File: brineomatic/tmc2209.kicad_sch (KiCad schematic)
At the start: 19 parts, among them J20 Conn_01x04, U9 TMC2209-LA

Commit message: updated jlc parts rotations and placement offsets
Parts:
- C39: LCSC C4967 -> C21122
- C42, J20: Rotation Offset (none) -> 180
- R53, U9: Rotation Offset (none) -> 270
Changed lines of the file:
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@@
+			)
+		)
+		(property "Rotation Offset" "180"
+			(at 152.4 57.15 0)
+			(effects
+				(font
+					(size 1.27 1.27)
+				)
+				(hide yes)
 			)
 		)
@@
 			)
 		)
+		(property "Rotation Offset" "270"
+			(at 81.28 105.41 0)
+			(effects
+				(font
+					(size 1.27 1.27)
+				)
+				(hide yes)
+			)
+		)
 		(pin "9"
 		)
@@
 		)
 		(property "LCSC" "C157926"
+			(at 109.22 110.49 0)
+			(effects
+				(font
+					(size 1.27 1.27)
+				)
+				(hide yes)
+			)
+		)
+		(property "Rotation Offset" "180"
 			(at 109.22 110.49 0)
 			(effects
@@
 			)
 		)
-		(property "LCSC" "C4967"
+		(property "LCSC" "C21122"
 			(at 104.14 95.25 90)
 			(effects
@@
 			(at 134.62 90.17 90)
 			(effects
+				(font
+					(size 1.27 1.27)
+				)
+				(hide yes)
+			)
+		)
+		(property "Rotation Offset" "270"
+			(at 134.62 90.17 90)
+			(effects

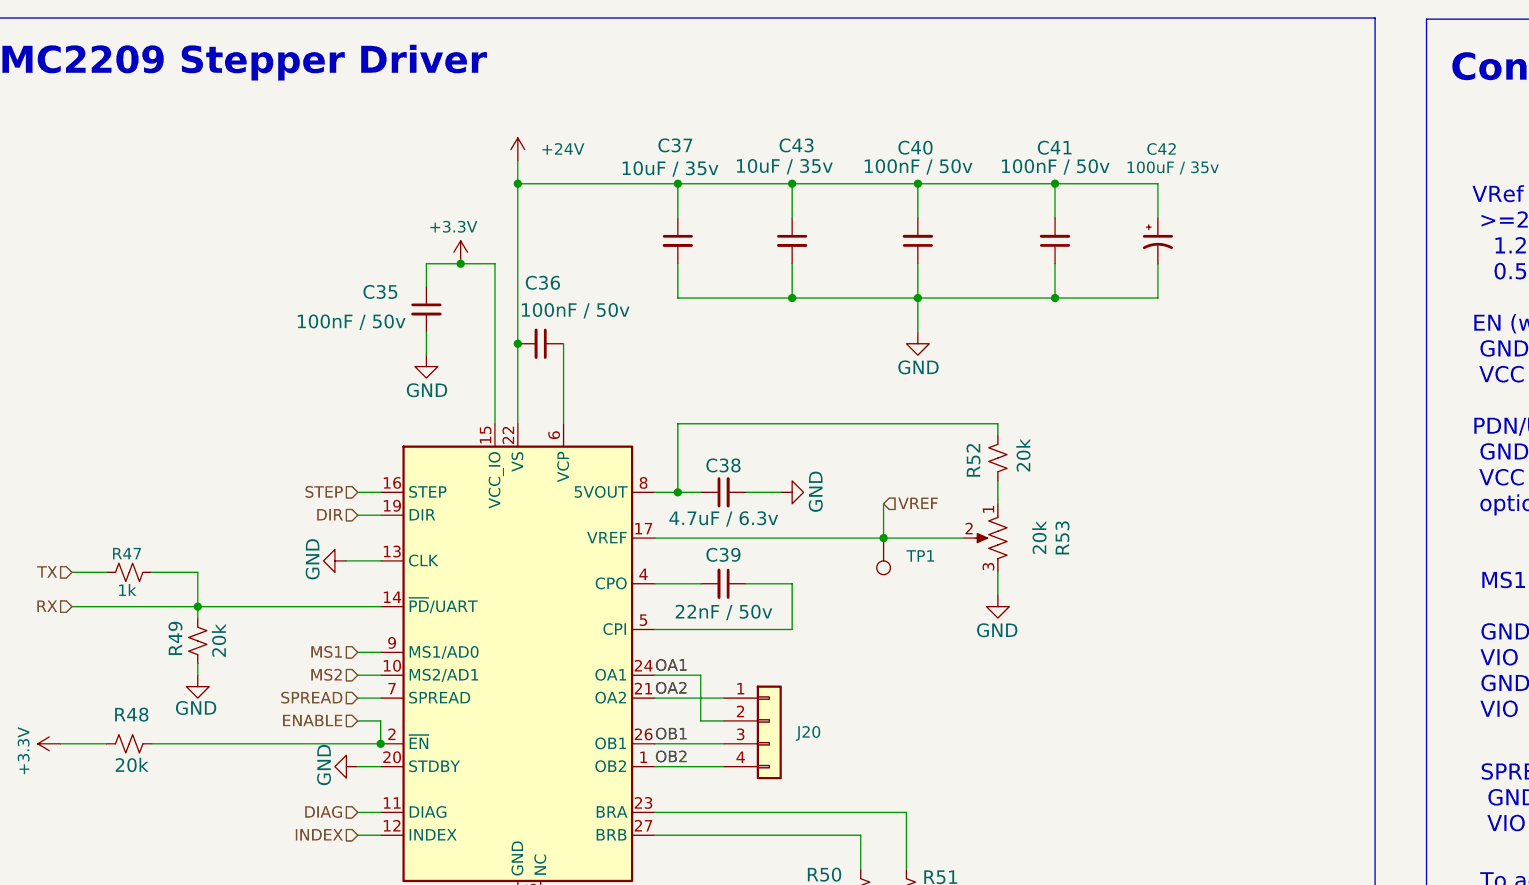
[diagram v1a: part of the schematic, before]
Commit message: via stitching, a couple minor changes, i think its ready for production
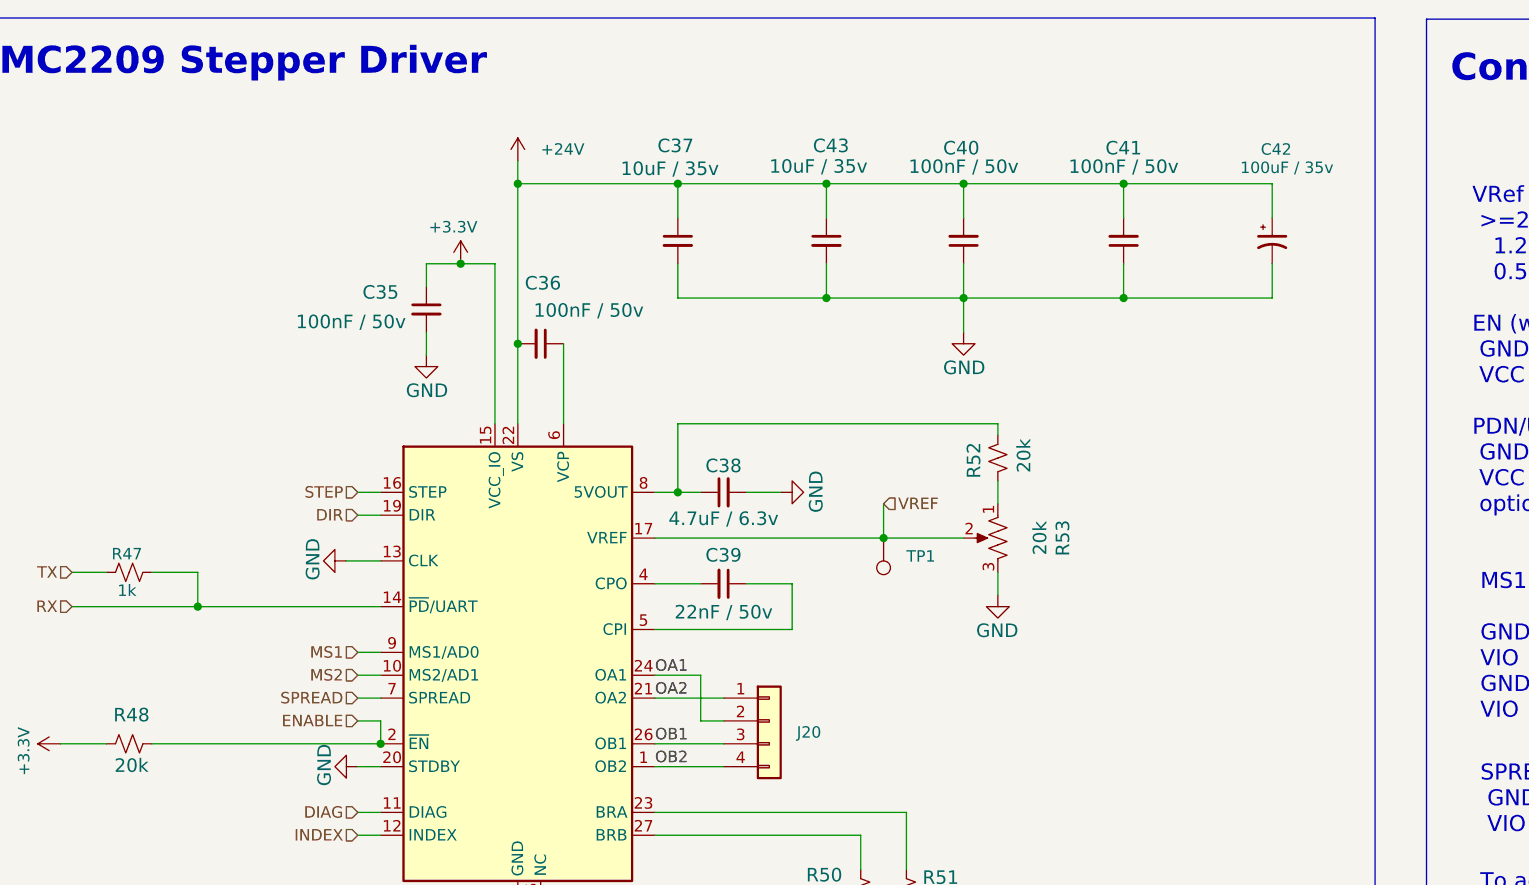
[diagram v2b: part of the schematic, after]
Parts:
- removed R49: 20k, Resistor_SMD:R_0603_1608Metric, symbol Device:R_Small_US
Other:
- moved on the sheet: C40, C41, C42, C43

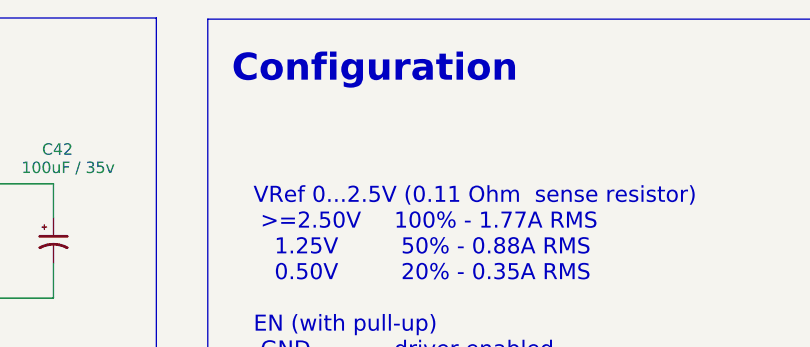
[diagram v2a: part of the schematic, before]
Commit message: added qwiic i2c connector
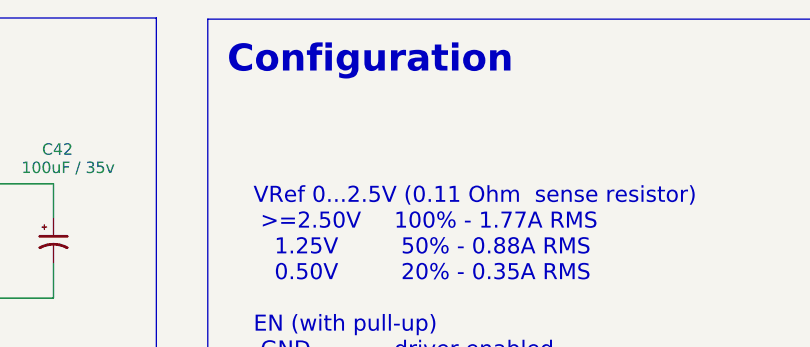
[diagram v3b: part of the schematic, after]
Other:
- title: (none) -> https://github.com/hoeken/brineomatic
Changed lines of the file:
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@@
 	(generator_version "9.0")
 	(paper "A4")
+	(title_block
+		(title "https://github.com/hoeken/brineomatic")
+		(date "2025-08-28")
+		(rev "B")
+	)
 	(rectangle
 		(start 18.415 32.385)
@@
 	(text "Configuration"
 		(exclude_from_sim no)
-		(at 184.912 38.1 0)
+		(at 184.404 37.084 0)
 		(effects
 			(font

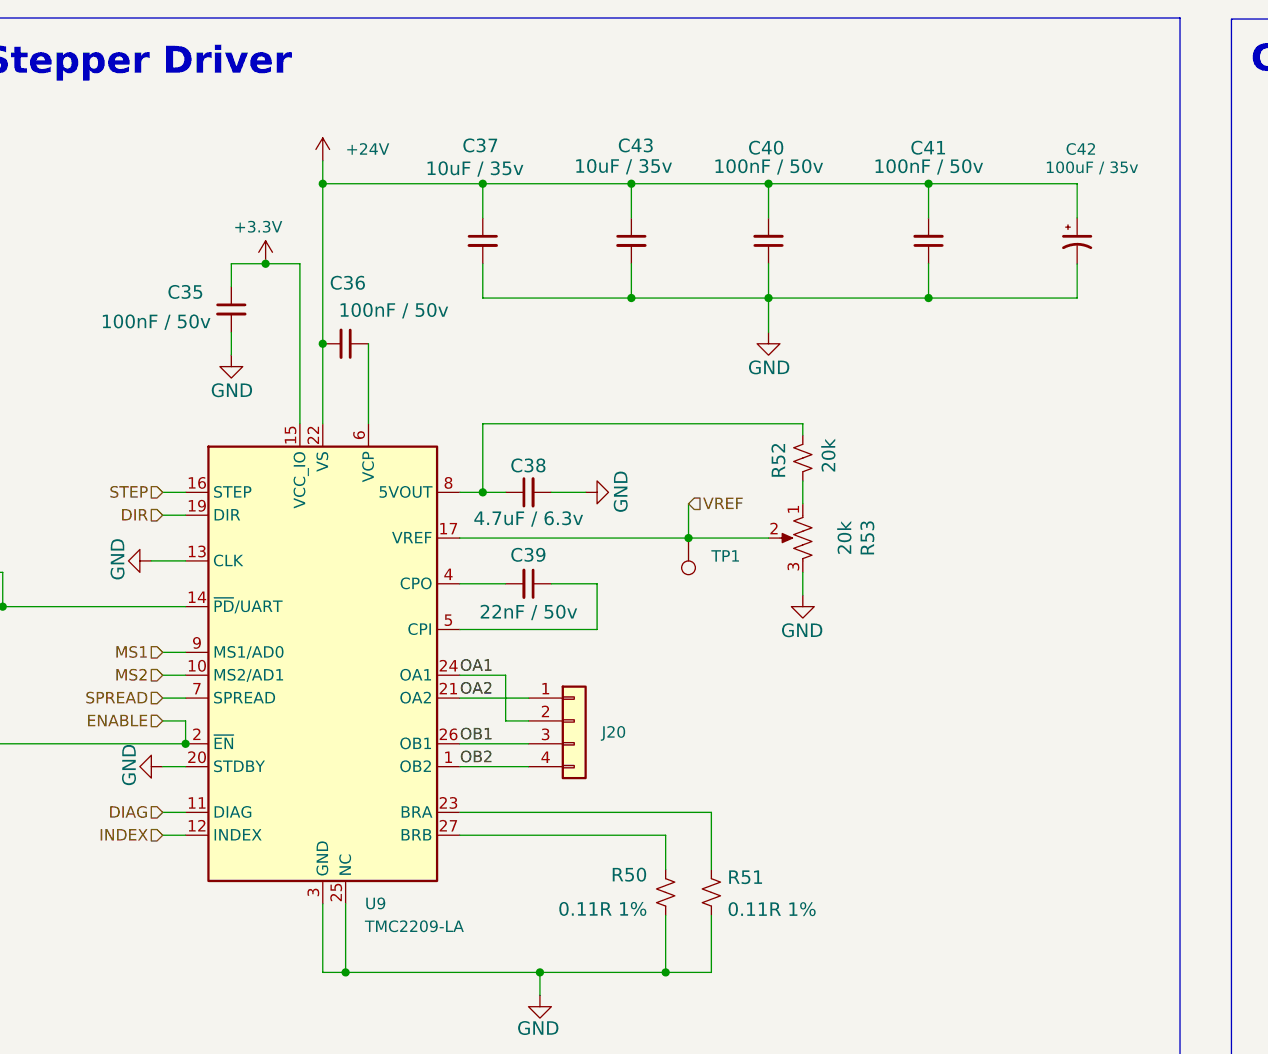
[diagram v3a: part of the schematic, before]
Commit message: added pullup resistor to adc alert
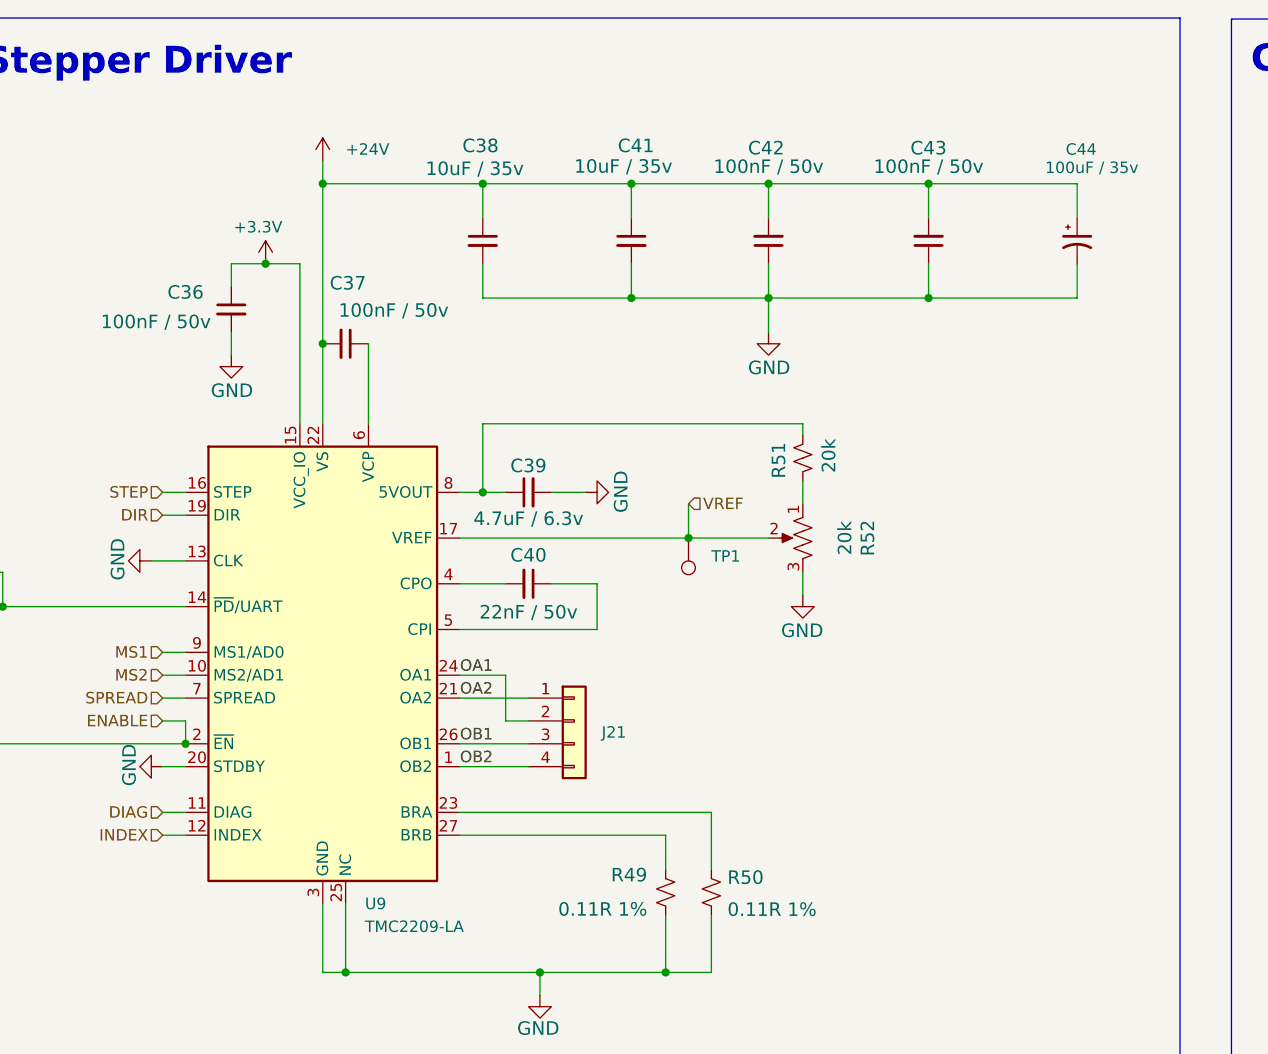
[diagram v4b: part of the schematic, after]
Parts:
- renumbered C35 to C36, C36 to C37, C37 to C38, C38 to C39, C39 to C40, C43 to C41, C40 to C42, C41 to C43, C42 to C44, J20 to J21, R50 to R49, R51 to R50, R52 to R51, R53 to R52
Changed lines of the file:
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@@
 		(on_board yes)
 		(dnp no)
-		(property "Reference" "#GND08"
+		(property "Reference" "#GND07"
 			(at 134.62 96.52 0)
 			(effects
@@
 			(project "brineomatic"
 				(path "/96477ae2-ef08-48f3-8dd4-fe4478541f68/0f01c39f-0c25-414e-9ed3-1ba09e2af0c5"
-					(reference "#GND08")
+					(reference "#GND07")
 					(unit 1)
 				)
@@
 		(on_board yes)
 		(dnp no)
-		(property "Reference" "#GND06"
+		(property "Reference" "#GND05"
 			(at 110.49 85.09 0)
 			(effects
@@
 			(project "brineomatic"
 				(path "/96477ae2-ef08-48f3-8dd4-fe4478541f68/0f01c39f-0c25-414e-9ed3-1ba09e2af0c5"
-					(reference "#GND06")
+					(reference "#GND05")
 					(unit 1)
 				)
@@
 		(on_board yes)
 		(dnp no)
-		(property "Reference" "#GND04"
+		(property "Reference" "#GND03"
 			(at 71.12 69.85 0)
 			(effects
@@
 			(project "brineomatic"
 				(path "/96477ae2-ef08-48f3-8dd4-fe4478541f68/0f01c39f-0c25-414e-9ed3-1ba09e2af0c5"
-					(reference "#GND04")
+					(reference "#GND03")
 					(unit 1)
 				)
@@
 		(on_board yes)
 		(dnp no)
-		(property "Reference" "C43"
+		(property "Reference" "C41"
 			(at 118.11 45.72 0)
 			(effects
@@
 			(project "brineomatic"
 				(path "/96477ae2-ef08-48f3-8dd4-fe4478541f68/0f01c39f-0c25-414e-9ed3-1ba09e2af0c5"
-					(reference "C43")
+					(reference "C41")
 					(unit 1)
 				)
@@
 		(on_board yes)
 		(dnp no)
-		(property "Reference" "#GND07"
+		(property "Reference" "#GND06"
 			(at 130.81 67.31 0)
 			(effects
@@
 			(project "brineomatic"
 				(path "/96477ae2-ef08-48f3-8dd4-fe4478541f68/0f01c39f-0c25-414e-9ed3-1ba09e2af0c5"
-					(reference "#GND07")
+					(reference "#GND06")
 					(unit 1)
 				)
@@
 		(on_board yes)
 		(dnp no)
-		(property "Reference" "C41"
+		(property "Reference" "C43"
 			(at 148.59 45.974 0)
 			(effects
@@
 			(project "brineomatic"
 				(path "/96477ae2-ef08-48f3-8dd4-fe4478541f68/0f01c39f-0c25-414e-9ed3-1ba09e2af0c5"
-					(reference "C41")
+					(reference "C43")
 					(unit 1)
 				)
@@
 		(on_board yes)
 		(dnp no)
-		(property "Reference" "R51"
+		(property "Reference" "R50"
 			(at 126.238 128.778 0)
 			(effects
@@
 			(project "brineomatic"
 				(path "/96477ae2-ef08-48f3-8dd4-fe4478541f68/0f01c39f-0c25-414e-9ed3-1ba09e2af0c5"
-					(reference "R51")
+					(reference "R50")
 					(unit 1)
 				)
@@
 		(on_board yes)
 		(dnp no)
-		(property "Reference" "C36"
+		(property "Reference" "C37"
 			(at 84.074 62.738 90)
 			(effects
@@
 			(project "brineomatic"
 				(path "/96477ae2-ef08-48f3-8dd4-fe4478541f68/0f01c39f-0c25-414e-9ed3-1ba09e2af0c5"
-					(reference "C36")
+					(reference "C37")
 					(unit 1)
 				)
@@
 		(on_board yes)
 		(dnp no)
-		(property "Reference" "C42"
+		(property "Reference" "C44"
 			(at 163.83 46.99 0)
 			(effects
@@
 			(project ""
 				(path "/96477ae2-ef08-48f3-8dd4-fe4478541f68/0f01c39f-0c25-414e-9ed3-1ba09e2af0c5"
-					(reference "C42")
+					(reference "C44")
 					(unit 1)
 				)
@@
 		(on_board yes)
 		(dnp no)
-		(property "Reference" "C37"
+		(property "Reference" "C38"
 			(at 100.838 45.72 0)
 			(effects
@@
 			(project "brineomatic"
 				(path "/96477ae2-ef08-48f3-8dd4-fe4478541f68/0f01c39f-0c25-414e-9ed3-1ba09e2af0c5"
-					(reference "C37")
+					(reference "C38")
 					(unit 1)
 				)
@@
 		(on_board yes)
 		(dnp no)
-		(property "Reference" "#GND02"
+		(property "Reference" "#GND01"
 			(at 62.23 92.71 0)
 			(effects
@@
 			(project "brineomatic"
 				(path "/96477ae2-ef08-48f3-8dd4-fe4478541f68/0f01c39f-0c25-414e-9ed3-1ba09e2af0c5"
-					(reference "#GND02")
+					(reference "#GND01")
 					(unit 1)
 				)
@@
 		(on_board yes)
 		(dnp no)
-		(property "Reference" "#PWR045"
+		(property "Reference" "#PWR047"
 			(at 74.93 63.5 0)
 			(effects
@@
 			(project "brineomatic"
 				(path "/96477ae2-ef08-48f3-8dd4-fe4478541f68/0f01c39f-0c25-414e-9ed3-1ba09e2af0c5"
-					(reference "#PWR045")
+					(reference "#PWR047")
 					(unit 1)
 				)
@@
 		(on_board yes)
 		(dnp no)
-		(property "Reference" "R50"
+		(property "Reference" "R49"
 			(at 117.348 126.746 0)
 			(effects
@@
 			(project "brineomatic"
 				(path "/96477ae2-ef08-48f3-8dd4-fe4478541f68/0f01c39f-0c25-414e-9ed3-1ba09e2af0c5"
-					(reference "R50")
+					(reference "R49")
 					(unit 1)
 				)
@@
 		(on_board yes)
 		(dnp no)
-		(property "Reference" "#PWR044"
+		(property "Reference" "#PWR046"
 			(at 34.29 113.03 0)
 			(effects
@@
 			(project "brineomatic"
 				(path "/96477ae2-ef08-48f3-8dd4-fe4478541f68/0f01c39f-0c25-414e-9ed3-1ba09e2af0c5"
-					(reference "#PWR044")
+					(reference "#PWR046")
 					(unit 1)
 				)
@@
 		(on_board yes)
 		(dnp no)
-		(property "Reference" "J20"
+		(property "Reference" "J21"
 			(at 112.268 111.76 0)
 			(effects
@@
 			(project ""
 				(path "/96477ae2-ef08-48f3-8dd4-fe4478541f68/0f01c39f-0c25-414e-9ed3-1ba09e2af0c5"
-					(reference "J20")
+					(reference "J21")
 					(unit 1)
 				)
@@
 		(on_board yes)
 		(dnp no)
-		(property "Reference" "C35"
+		(property "Reference" "C36"
 			(at 66.04 63.754 0)
 			(effects
@@
 			(project "brineomatic"
 				(path "/96477ae2-ef08-48f3-8dd4-fe4478541f68/0f01c39f-0c25-414e-9ed3-1ba09e2af0c5"
-					(reference "C35")
+					(reference "C36")
 					(unit 1)
 				)
@@
 		(dnp no)
 		(fields_autoplaced yes)
-		(property "Reference" "#PWR046"
+		(property "Reference" "#PWR048"
 			(at 81.28 52.07 0)
 			(effects
@@
 			(project ""
 				(path "/96477ae2-ef08-48f3-8dd4-fe4478541f68/0f01c39f-0c25-414e-9ed3-1ba09e2af0c5"
-					(reference "#PWR046")
+					(reference "#PWR048")
 					(unit 1)
 				)
@@
 		(on_board yes)
 		(dnp no)
-		(property "Reference" "R52"
+		(property "Reference" "R51"
 			(at 132.842 81.534 90)
 			(effects
@@
 			(project "brineomatic"
 				(path "/96477ae2-ef08-48f3-8dd4-fe4478541f68/0f01c39f-0c25-414e-9ed3-1ba09e2af0c5"
-					(reference "R52")
+					(reference "R51")
 					(unit 1)
 				)
@@
 		(on_board yes)
 		(dnp no)
-		(property "Reference" "C39"
+		(property "Reference" "C40"
 			(at 104.14 92.964 90)
 			(effects
@@
 			(project "brineomatic"
 				(path "/96477ae2-ef08-48f3-8dd4-fe4478541f68/0f01c39f-0c25-414e-9ed3-1ba09e2af0c5"
-					(reference "C39")
+					(reference "C40")
 					(unit 1)
 				)
@@
 		(on_board yes)
 		(dnp no)
-		(property "Reference" "#GND05"
+		(property "Reference" "#GND04"
 			(at 105.41 140.97 0)
 			(effects
@@
 			(project "brineomatic"
 				(path "/96477ae2-ef08-48f3-8dd4-fe4478541f68/0f01c39f-0c25-414e-9ed3-1ba09e2af0c5"
-					(reference "#GND05")
+					(reference "#GND04")
 					(unit 1)
 				)
@@
 		(on_board yes)
 		(dnp no)
-		(property "Reference" "C38"
+		(property "Reference" "C39"
 			(at 104.14 81.28 90)
 			(effects
@@
 			(project "brineomatic"
 				(path "/96477ae2-ef08-48f3-8dd4-fe4478541f68/0f01c39f-0c25-414e-9ed3-1ba09e2af0c5"
-					(reference "C38")
+					(reference "C39")
 					(unit 1)
 				)
@@
 		(on_board yes)
 		(dnp no)
-		(property "Reference" "#GND03"
+		(property "Reference" "#GND02"
 			(at 63.5 115.57 0)
 			(effects
@@
 			(project "brineomatic"
 				(path "/96477ae2-ef08-48f3-8dd4-fe4478541f68/0f01c39f-0c25-414e-9ed3-1ba09e2af0c5"
-					(reference "#GND03")
+					(reference "#GND02")
 					(unit 1)
 				)
@@
 		(on_board yes)
 		(dnp no)
-		(property "Reference" "R53"
+		(property "Reference" "R52"
 			(at 140.97 90.17 90)
 			(effects
@@
 			(project "brineomatic"
 				(path "/96477ae2-ef08-48f3-8dd4-fe4478541f68/0f01c39f-0c25-414e-9ed3-1ba09e2af0c5"
-					(reference "R53")
+					(reference "R52")
 					(unit 1)
 				)
@@
 		(on_board yes)
 		(dnp no)
-		(property "Reference" "C40"
+		(property "Reference" "C42"
 			(at 130.556 45.974 0)
 			(effects
@@
 			(project "brineomatic"
 				(path "/96477ae2-ef08-48f3-8dd4-fe4478541f68/0f01c39f-0c25-414e-9ed3-1ba09e2af0c5"
-					(reference "C40")
-					(unit 1)
-				)
+					(reference "C42")
+					(unit 1)
+				)
